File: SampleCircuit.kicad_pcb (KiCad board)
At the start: 2 copper layers, 100 x 90 mm, 50 parts, among them J1 24V INPUT, J2 12V TEST, J3 5V TEST, J4 3.3V TEST, J5 SPEAKER, SW1 RESET, SW2 BOOT, U1 LMZM23601SILR, U15 TLV803S, U2 ESP32-S3-WROOM-1, U23 RV-3028-C7, U24 LMZM23601SILR, U25 LMZM23601SILR, U5 NS4168, U6 MicroSD

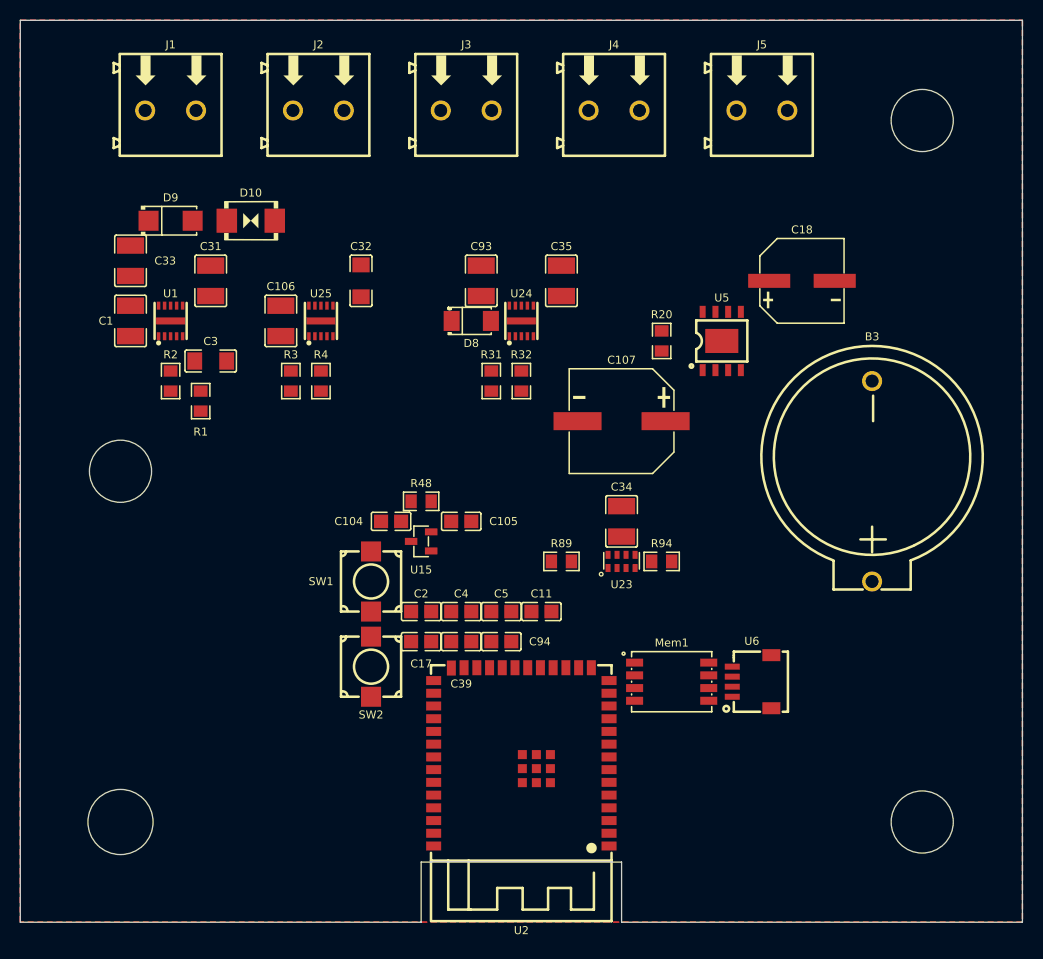
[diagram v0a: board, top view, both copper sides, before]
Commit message: Move to proper 4-corner mounting holes, prioritize holes in spec
- Replace ML(110,91) with TL(110,56) corner hole
- Shift J1-J5 connectors right to clear TL keepout (13mm even spacing)
- Shift D9/D10 input protection to follow J1
- Spec updates:
  - Rule 2g: mounting holes have HIGHEST placement priority
  - Rule 2h: verification checklist for hole placement
  - Section 8b: reorder workflow to place holes BEFORE components
- All 4 holes at proper corners: TL(110,56) TR(190,56) BL(110,126) BR(190,126)
- All verification checks pass (0 errors, 7 warnings)

Co-Authored-By: Claude Opus 4.6 <noreply@anthropic.com>
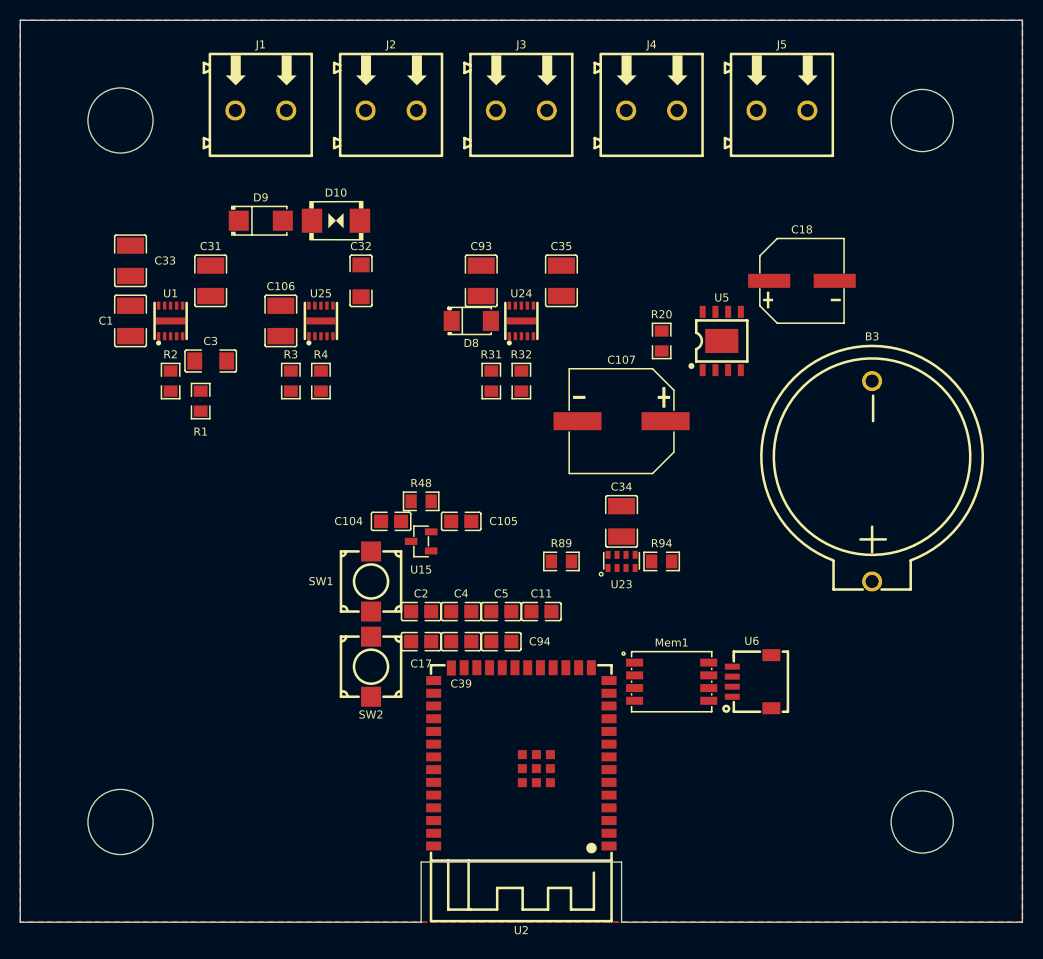
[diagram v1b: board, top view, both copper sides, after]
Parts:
- moved D9 9.00 mm to (124.0, 66.0)
- moved J1 9.00 mm to (124.0, 55.0)
- moved D10 8.50 mm to (131.5, 66.0)
- moved J2 7.25 mm to (137.0, 55.0)
- moved J3 5.50 mm to (150.0, 55.0)
- moved J4 3.75 mm to (163.0, 55.0)
- moved J5 2.00 mm to (176.0, 55.0)
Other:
- outline, holes or cut-outs redrawn
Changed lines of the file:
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@@
 	(footprint "JLCImport:SMBJ26CA_C89651"
 		(layer "F.Cu")
-		(at 123 66)
+		(at 131.5 66)
 		(descr "SMBJ26CA; SMB_L4.6-W3.6-LS5.3-BI; TVS Diode 26V Bidirectional")
 		(tags "C89651 SMBJ26CA SMB_L4.6-W3.6-LS5.3-BI TVS")
@@
 	(footprint "JLCImport:WJ500V-5_08-2P-14-00A"
 		(layer "F.Cu")
-		(at 115 55)
+		(at 124 55)
 		(descr "WJ500V-5.08-2P")
 		(tags "C8465 CONN-TH_2P-P5.00_WJ500V-5.08-2P KANGNEX WJ500V-5.08-2P")
@@
 	(footprint "JLCImport:WJ500V-5_08-2P-14-00A"
 		(layer "F.Cu")
-		(at 159.25 55)
+		(at 163 55)
 		(descr "WJ500V-5.08-2P")
 		(tags "C8465 CONN-TH_2P-P5.00_WJ500V-5.08-2P KANGNEX WJ500V-5.08-2P")
@@
 	(footprint "JLCImport:SS34_C8678"
 		(layer "F.Cu")
-		(at 115 66)
+		(at 124 66)
 		(descr "SS34")
 		(tags "C8678 MDD SMA_L4.3-W2.6-LS5.2-RD SS34")
@@
 	(footprint "JLCImport:WJ500V-5_08-2P-14-00A"
 		(layer "F.Cu")
-		(at 129.75 55)
+		(at 137 55)
 		(descr "WJ500V-5.08-2P")
 		(tags "C8465 CONN-TH_2P-P5.00_WJ500V-5.08-2P KANGNEX WJ500V-5.08-2P")
@@
 	(footprint "JLCImport:WJ500V-5_08-2P-14-00A"
 		(layer "F.Cu")
-		(at 174 55)
+		(at 176 55)
 		(descr "WJ500V-5.08-2P")
 		(tags "C8465 CONN-TH_2P-P5.00_WJ500V-5.08-2P KANGNEX WJ500V-5.08-2P")
@@
 	(footprint "JLCImport:WJ500V-5_08-2P-14-00A"
 		(layer "F.Cu")
-		(at 144.5 55)
+		(at 150 55)
 		(descr "WJ500V-5.08-2P")
 		(tags "C8465 CONN-TH_2P-P5.00_WJ500V-5.08-2P KANGNEX WJ500V-5.08-2P")
@@
 		)
 	)
+	(gr_circle
+		(center 110 56)
+		(end 113.25 56)
+		(stroke
+			(width 0.05)
+			(type default)
+		)
+		(fill no)
+		(layer "Edge.Cuts")
+	)
 	(gr_line
 		(start 200 46)
@@
 		(layer "Edge.Cuts")
 	)
-	(gr_circle
-		(center 110 91)
-		(end 113.1 91)
-		(stroke
-			(width 0.05)
-			(type default)
-		)
-		(fill no)
-		(layer "Edge.Cuts")
-	)
 	(gr_line
 		(start 100 136)
@@
 		(min_thickness 0.25)
 		(filled_areas_thickness no)
-		(fill
+		(fill yes
 			(thermal_gap 0)
 			(thermal_bridge_width 0)
@@
 		(min_thickness 0.25)
 		(filled_areas_thickness no)
-		(fill
+		(fill yes
 			(thermal_gap 0)
 			(thermal_bridge_width 0)

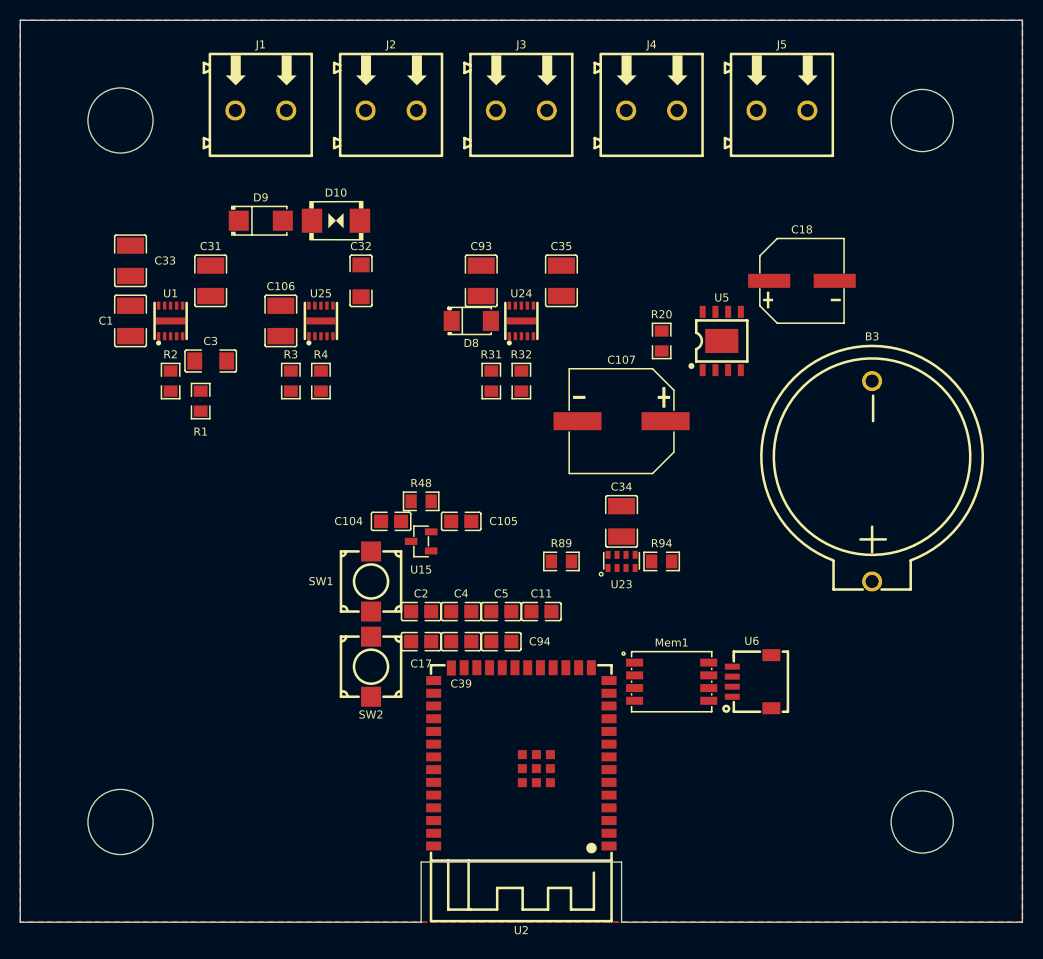
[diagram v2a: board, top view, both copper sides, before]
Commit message: Autoroute board with net classes, add routing spec section 13
- Add net classes: Power (0.5mm), Signal (0.25mm), Default (0.25mm)
- Assign +24V/+12V/+5V/+3.3V to Power class
- Autoroute via Freerouting: 367 tracks, 32 vias, 3 unrouted
- New spec section 13 (Autorouting):
  - 13a: placement and routing are independent operations
  - 13b: net class definitions with fabricator minimum tables
  - 13c: net class assignment rules
  - 13d: Freerouting workflow (DSN export/import)
  - 13e: post-routing review checklist
  - 13f: re-routing policy (explicit user decision only)

Co-Authored-By: Claude Opus 4.6 <noreply@anthropic.com>
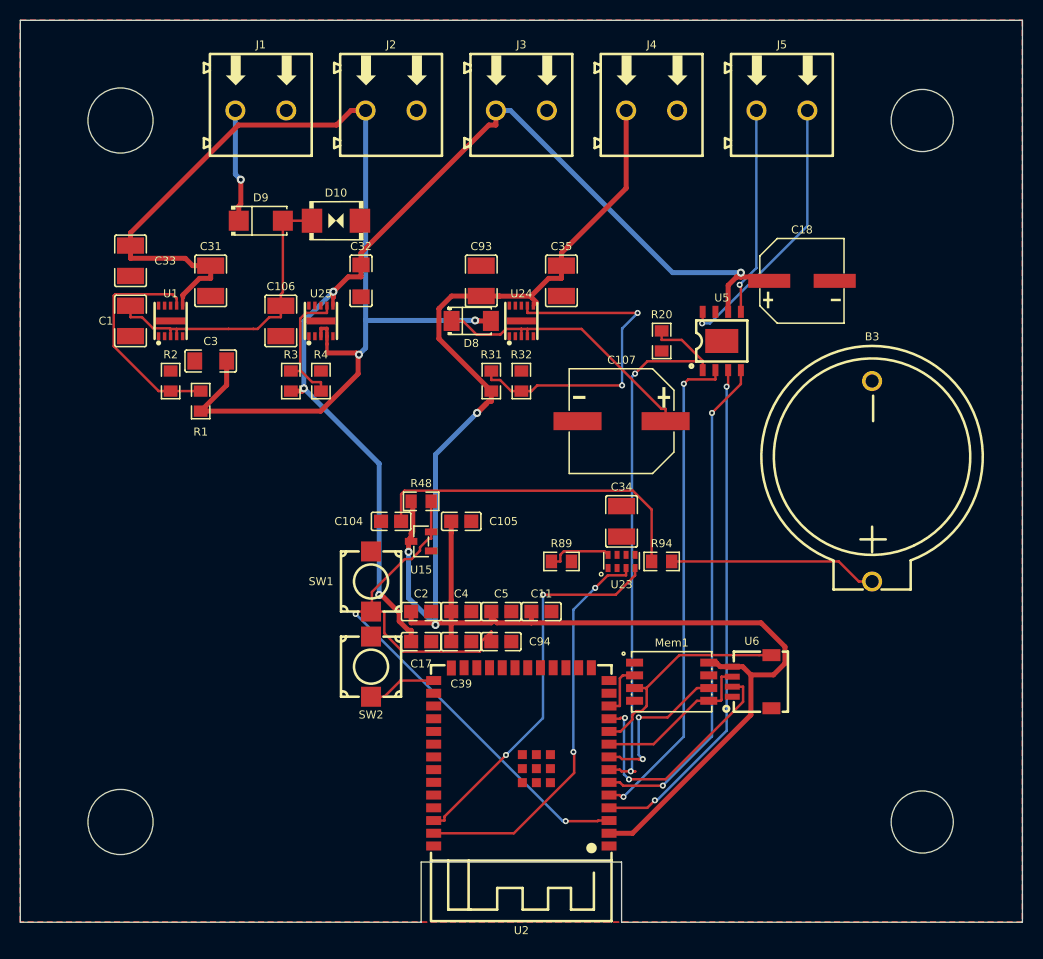
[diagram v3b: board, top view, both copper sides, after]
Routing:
- net +3.3V: track 0.00 -> 177.3 mm, vias 0 -> 3
- net +12V: track 0.00 -> 114.6 mm, vias 0 -> 2
- net +5V: track 0.00 -> 108.5 mm, vias 0 -> 4
- net Enable: track 0.00 -> 67.0 mm, vias 0 -> 2
- net AMP_EN: track 0.00 -> 57.2 mm, vias 0 -> 2
- net BCLK: track 0.00 -> 51.0 mm, vias 0 -> 2
- net DIN: track 0.00 -> 50.2 mm, vias 0 -> 2
- net LRCLK: track 0.00 -> 49.5 mm, vias 0 -> 2
- net SCL: track 0.00 -> 40.2 mm, vias 0 -> 2
- net SDA: track 0.00 -> 38.4 mm, vias 0 -> 2
- net Net-(U24-FB): track 0.00 -> 34.2 mm, vias 0 -> 2
- net Net-(U23-VBACKUP): track 0.00 -> 33.8 mm
- net Net-(D10-K): track 0.00 -> 31.2 mm
- net Net-(D8-K): track 0.00 -> 28.1 mm
- net OUTP: track 0.00 -> 27.2 mm, vias 0 -> 1
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
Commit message: Fix duplicate GND zone on F.Cu, add zone layer rules to spec
- Move second GND zone from F.Cu to B.Cu (fixes DRC intersection error)
- Spec rule 7b: one copper zone per layer, never duplicate layer+priority
- Spec rule 7e: clarify keepout rule areas vs copper zones
- Spec rule 7h: zone verification checklist
- Add S7 duplicate zone check to verification script

Co-Authored-By: Claude Opus 4.6 <noreply@anthropic.com>
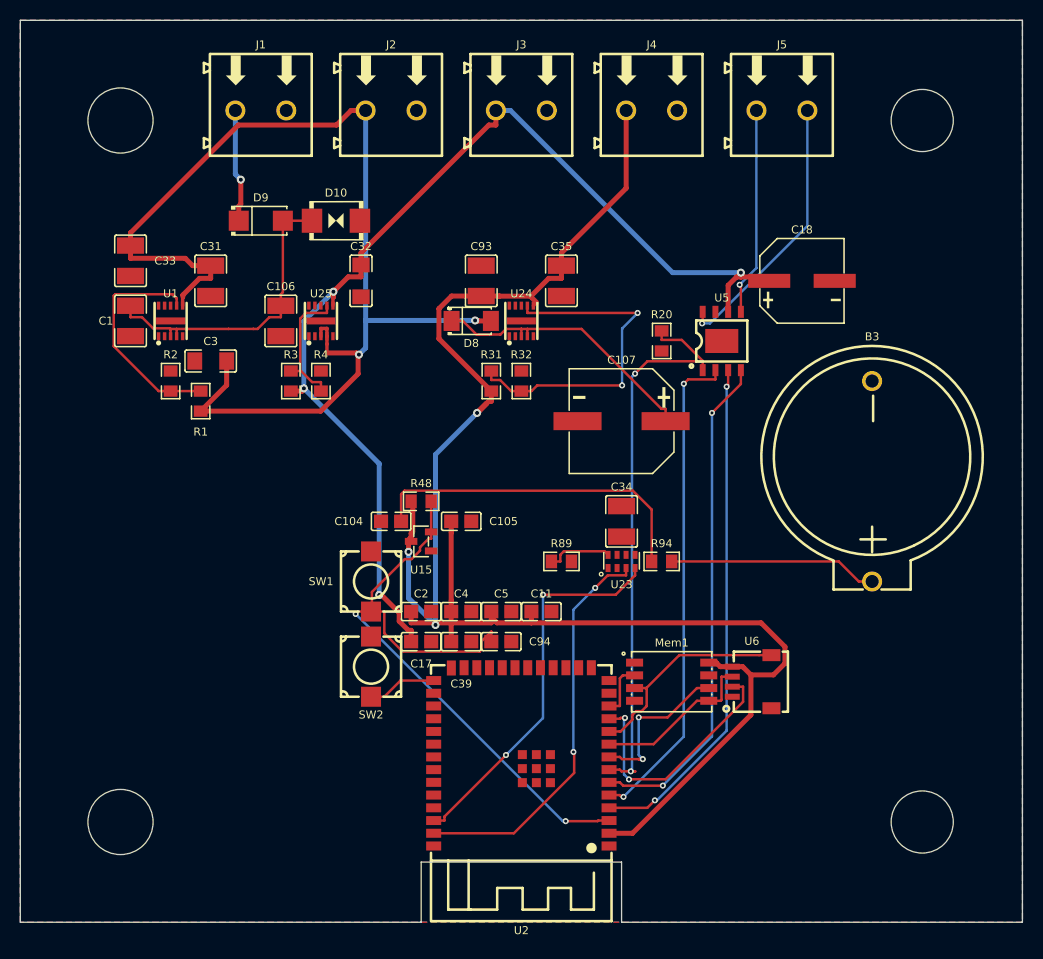
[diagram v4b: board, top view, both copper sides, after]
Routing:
- added copper zone on B.Cu, net GND
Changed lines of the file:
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@@
-	)
-	(zone
-		(net 2)
-		(net_name "GND")
-		(layer "F.Cu")
-		(name "GND")
-		(hatch edge 0.5)
-		(connect_pads
-			(clearance 0)
-		)
-		(min_thickness 0.25)
-		(filled_areas_thickness no)
-		(fill yes
-			(thermal_gap 0)
-			(thermal_bridge_width 0)
-		)
-		(polygon
-			(pts
-				(xy 100 46) (xy 200 46) (xy 200 136) (xy 100 136)
-			)
-		)
 	)
 	(zone
@@
 			)
 		)
+	)
+	(zone
+		(net 2)
+		(net_name "GND")
+		(layer "B.Cu")
+		(name "GND")
+		(hatch edge 0.5)
+		(connect_pads
+			(clearance 0)
+		)
+		(min_thickness 0.25)
+		(filled_areas_thickness no)
+		(fill yes
+			(thermal_gap 0)
+			(thermal_bridge_width 0)
+		)
+		(polygon
+			(pts
+				(xy 100 46) (xy 200 46) (xy 200 136) (xy 100 136)
+			)
+		)
